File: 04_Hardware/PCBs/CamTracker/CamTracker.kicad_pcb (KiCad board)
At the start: 6 copper layers, 80 x 97.3 mm, 345 parts, among them IC1 W25Q128JVSIM, IC3 AP64502QSP-13, J1 PJ-059A, J10 67996-100HLF, J11 22-28-4044, J12 22-28-4044, J13 22-28-4044, J14 22-28-4044, J15 67996-100HLF, J16 SIM8066-6-1-14-01-A, J17 MEM2061-01-188-00-A, J18 636101112001, J19 636101112001, J2 22-28-4044, J20 636101112001, J21 636101112001, J22 22-28-4034, J23 22-28-4044, J24 22-28-4034, J25 1.25x15P, J26 1.25x15P, J27 53047-0210, J3 USB3076-30-A, J4 67996-100HLF, J5 USB4080-03-A, J6 22-28-4034, J7 22-28-4034, J8 67996-100HLF, J9 22-28-4034, Q1 BC817-40,215, Q10 BC817-40,215, Q11 BC817-40,215, Q12 BC817-40,215, Q2 BC817-40,215, Q4 BC817-40,215, Q5 BC817-40,215, Q6 BC817-40,215, Q7 BC817-40,215, Q8 BC817-40,215, Q9 BC817-40,215, U1 SC206EEMDA-G51-UGNDA, U2 SGM804, U3 AP7335-WG-7, U4 AP61100Z6-7, U5 PAM8302AASCR, U6 ST4SI2M0020TPIFW, U7 RP2040, U8 AP61100Z6-7, Y1 ABM8-272-T3

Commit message: feat: Completed Placement v1 in Layout
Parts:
- removed C38, C39, C49, C50, C72: 100nF 10V, 000MCLib:CAPC1005X55N
- removed C47: 22uF 6.3V, 000MCLib:CAPC1005X55N
- removed C48: 10uF 6.3V, 000MCLib:CAPC1005X55N
- removed C71, C76: 1uF 50V, 000MCLib:CAPC1005X55N
- removed C74: 47uF 10V X7S, 000MCLib:CAPC3225X280N
- removed D1: SMBJ20A, 000MCLib:DIOM5436X244N
- removed D10, D31: SP0402U-ULC-02ETG, 000MCLib:SESD0402Q2UG0020090
- removed D14, D15, D16, D32: SC1205-01ETG, 000MCLib:SC120501ETG
- removed D17: RB751S40, 000MCLib:SOD1608X70
- removed FL7, FL8: LCFE121002A900TG, 000MCLib:LCFE121002A900TG
- removed J19, J20: 636101112001, 000MCLib:COAX2_636101112001_WRE
- removed J25: 1.25x15P, 000MCLib:CONN-SMD_15P-P1.25_HCTL_HC-1.25-15PLT
- removed J8: 67996-100HLF, 000MCLib:HDRV2W67P254_2X1_254X483X858P
- removed L3: 74404024010, 000MCLib:IND_WE-LQS_2512_WRE
- removed Q12, Q7, Q8: BC817-40,215, 000MCLib:BC81740215
- removed R21: 0R, 000MCLib:RESC2012X50N
- removed R22, R47, R48, R51, R53, R86: 10K, 000MCLib:RC0402N_YAG
- removed R28: 1K, 000MCLib:RC0402N_YAG
- removed R50: 4K7, 000MCLib:RC0402N_YAG
- removed R88: 0R, 000MCLib:RC0402N_YAG
- removed REF**: Polarity_Center_Positive_6mm_SilkScreen, Symbol:Polarity_Center_Positive_6mm_SilkScreen
- removed TP56: TestPoint, TestPoint:TestPoint_Pad_D1.0mm
- removed U5: PAM8302AASCR, 000MCLib:SOP65P490X110-8N
- removed U8: AP61100Z6-7, 000MCLib:SOT50P162X60-6N
- added C100: 33pF 50V, 000MCLib:CAPC1005X55N, F.Cu at (163.6, 79.6)
- added C102: 100nF 10V, 000MCLib:CAPC1005X55N, F.Cu at (164.1, 82.2)
- added C103: 10pF 50V, 000MCLib:CAPC1005X55N, F.Cu at (164.6, 79.6)
- added C105: 22uF 6.3V, 000MCLib:CAPC1005X55N, F.Cu at (95.0, 67.1)
- added C108: 33pF 50V, 000MCLib:CAPC1005X55N, F.Cu at (97.5, 64.4)
- added C109: 33pF 50V, 000MCLib:CAPC1005X55N, F.Cu at (92.8, 63.3)
- added C110: 33pF 50V, 000MCLib:CAPC1005X55N, F.Cu at (97.5, 63.3)
- added C111: 100nF 10V, 000MCLib:CAPC1005X55N, B.Cu at (100.9, 95.3)
- added C112: 1uF 50V, 000MCLib:CAPC1005X55N, B.Cu at (101.9, 95.3)
- added C113: 1uF 50V, 000MCLib:CAPC1005X55N, B.Cu at (98.8, 99.5)
- added C114: 22uF 25V, 000MCLib:CAPC2012X145N, B.Cu at (188.6, 103.0)
- added C115: 100nF 10V, 000MCLib:CAPC1005X55N, B.Cu at (183.4, 104.7)
- added C116: 22uF 25V, 000MCLib:CAPC2012X145N, B.Cu at (185.4, 103.0)
- added C118: 220nF 10V, 000MCLib:CAPC1005X55N, B.Cu at (190.5, 69.5)
- added C119: 220nF 10V, 000MCLib:CAPC1005X55N, B.Cu at (190.5, 70.6)
- added C120: 220nF 10V, 000MCLib:CAPC1005X55N, B.Cu at (190.5, 71.7)
- added C121: 220nF 10V, 000MCLib:CAPC1005X55N, B.Cu at (190.5, 72.7)
- added C122: 10uF 50V X7R, 000MCLib:CAPC3216X190N, B.Cu at (190.7, 67.8)
- added C123: 10uF 50V X7R, 000MCLib:CAPC3216X190N, B.Cu at (190.7, 65.4)
- added C124: 10uF 50V X7R, 000MCLib:CAPC3216X190N, B.Cu at (190.7, 63.1)
- added C125: 100nF 10V, 000MCLib:CAPC1005X55N, B.Cu at (175.9, 63.9)
- added C126: 100nF 10V, 000MCLib:CAPC1005X55N, B.Cu at (176.7, 100.0)
- added C127: 100nF 10V, 000MCLib:CAPC1005X55N, B.Cu at (176.7, 86.8)
- added C128: 100nF 10V, 000MCLib:CAPC1005X55N, B.Cu at (190.1, 93.6)
- added C129: 100nF 10V, 000MCLib:CAPC1005X55N, B.Cu at (186.7, 100.4)
- added C130: 100nF 10V, 000MCLib:CAPC1005X55N, B.Cu at (174.0, 93.1)
- added C131: 100nF 10V, 000MCLib:CAPC1005X55N, B.Cu at (190.1, 91.2)
- added C132: 100nF 10V, 000MCLib:CAPC1005X55N, B.Cu at (184.0, 87.2)
- added C133: 100nF 10V, 000MCLib:CAPC1005X55N, B.Cu at (183.4, 102.9)
- added C134: 100nF 10V, 000MCLib:CAPC1005X55N, B.Cu at (174.1, 94.2)
- added C135: 100nF 10V, 000MCLib:CAPC1005X55N, B.Cu at (181.0, 86.1)
- added C136: 2.2uF 10V, 000MCLib:CAPC1608X90N, B.Cu at (190.3, 96.5)
- added C137: 22uF 25V, 000MCLib:CAPC2012X145N, B.Cu at (173.8, 86.8)
- added C138: 2.2uF 10V, 000MCLib:CAPC1608X90N, B.Cu at (190.3, 97.9)
- added C139: 100nF 10V, 000MCLib:CAPC1005X55N, B.Cu at (190.1, 95.3)
- added C140: 100nF 10V, 000MCLib:CAPC1005X55N, B.Cu at (190.1, 99.1)
- added C141: 100nF 10V, 000MCLib:CAPC1005X55N, B.Cu at (185.5, 100.4)
- added C142: 100nF 10V, 000MCLib:CAPC1005X55N, B.Cu at (174.0, 100.6)
- added C143: 220nF 10V, 000MCLib:CAPC1005X55N, B.Cu at (182.7, 100.4)
- added C144: 220nF 10V, 000MCLib:CAPC1005X55N, B.Cu at (181.7, 100.4)
- added C145: 220nF 10V, 000MCLib:CAPC1005X55N, B.Cu at (179.7, 100.4)
- added C146: 220nF 10V, 000MCLib:CAPC1005X55N, B.Cu at (180.7, 100.4)
- added C147: 100nF 10V, 000MCLib:CAPC1005X55N, B.Cu at (174.0, 99.6)
- added C148: 10pF 50V, 000MCLib:CAPC1005X55N, B.Cu at (171.2, 96.8)
- added C149: 1uF 50V, 000MCLib:CAPC1005X55N, B.Cu at (173.9, 89.5)
- added D19: SC1205-01ETG, 000MCLib:SC120501ETG, F.Cu at (117.6, 64.3)
- added D28: SC1205-01ETG, 000MCLib:SC120501ETG, F.Cu at (179.7, 87.6)
- added D29: SC1205-01ETG, 000MCLib:SC120501ETG, F.Cu at (193.1, 87.6)
- added FL4: LCFE121002A900TG, 000MCLib:LCFE121002A900TG, F.Cu at (178.7, 80.2)
- added FL5: LCFE121002A900TG, 000MCLib:LCFE121002A900TG, F.Cu at (178.7, 77.9)
- added IC2: AP7361E-33FGE-7, 000MCLib:SON65P300X300X63-9N, B.Cu at (116.2, 89.3)
- added J28: Bus_M.2_Socket_M, 000MCLib:121992304, B.Cu at (182.7, 72.0)
- added L10: 1uH 2.2A, 000MCLib:IND_WE-LQS_2512_WRE, B.Cu at (101.3, 90.0)
- added LED2: SML-P11VTT86R, 000MCLib:SMLP11VTT86R, F.Cu at (86.5, 64.5)
- added LED5: SML-P11VTT86R, 000MCLib:SMLP11VTT86R, B.Cu at (171.4, 91.9)
- added Q3: BC817-40,215, 000MCLib:BC81740215, F.Cu at (107.4, 67.0)
- added R113: 10K, 000MCLib:RC0402N_YAG, B.Cu at (189.9, 105.8)
- added R114: 10K, 000MCLib:RC0402N_YAG, B.Cu at (101.4, 87.5)
- added R115: 10K, 000MCLib:RC0402N_YAG, B.Cu at (173.9, 88.4)
- added R116: 10K, 000MCLib:RC0402N_YAG, B.Cu at (191.9, 91.7)
- added R117: 0R, 000MCLib:RC0402N_YAG, B.Cu at (190.1, 88.9)
- added R118: 0R, 000MCLib:RC0402N_YAG, B.Cu at (190.1, 90.1)
- added R119: 1K, 000MCLib:RC0402N_YAG, B.Cu at (172.7, 60.5)
- added R120: 10K, 000MCLib:RC0402N_YAG, B.Cu at (170.1, 61.7)
- added R121: 10K, 000MCLib:RC0402N_YAG, B.Cu at (190.3, 60.0)
- added R122: 0R, 000MCLib:RC0402N_YAG, B.Cu at (190.3, 61.3)
- added R123: 0R, 000MCLib:RC0402N_YAG, B.Cu at (172.8, 61.7)
- added R124: 4K7, 000MCLib:RC0402N_YAG, B.Cu at (190.1, 87.7)
- added R125: 12K1, 000MCLib:RC0402N_YAG, B.Cu at (175.7, 100.0)
- added R126: 100K, 000MCLib:RC0402N_YAG, B.Cu at (173.8, 90.7)
- added R127: 200K, 000MCLib:RC0402N_YAG, B.Cu at (98.1, 91.7)
- added R16: 0R, 000MCLib:RESC2012X50N, B.Cu at (109.6, 85.7)
- added R69: 33R, 000MCLib:RC0402N_YAG, F.Cu at (186.4, 89.9)
- added R73: 33R, 000MCLib:RC0402N_YAG, F.Cu at (190.4, 89.9)
- added R74: 10K, 000MCLib:RC0402N_YAG, F.Cu at (167.7, 87.3)
- added R75: 100K, 000MCLib:RC0402N_YAG, F.Cu at (169.7, 86.6)
- added R76: 51K, 000MCLib:RC0402N_YAG, F.Cu at (187.7, 89.9)
- added R77: 51K, 000MCLib:RC0402N_YAG, F.Cu at (182.4, 89.9)
- added R78: 51K, 000MCLib:RC0402N_YAG, F.Cu at (181.0, 89.9)
- added TP23: TestPoint, TestPoint:TestPoint_Pad_D1.0mm, F.Cu at (117.5, 74.4)
- added TP24: TestPoint, TestPoint:TestPoint_Pad_D1.0mm, F.Cu at (115.3, 74.4)
- added TP25: TestPoint, TestPoint:TestPoint_Pad_D1.0mm, F.Cu at (117.6, 72.3)
- added TP26: TestPoint, TestPoint:TestPoint_Pad_D1.0mm, F.Cu at (115.4, 72.3)
- added TP33: TestPoint, TestPoint:TestPoint_Pad_D1.0mm, B.Cu at (102.6, 99.8)
- added TP39: 3.86V, TestPoint:TestPoint_Pad_D1.0mm, B.Cu at (187.5, 96.3)
- added TP40: 3.86V, TestPoint:TestPoint_Pad_D1.0mm, B.Cu at (175.8, 84.9)
- added TP43: TestPoint, TestPoint:TestPoint_Pad_D1.0mm, B.Cu at (133.2, 66.9)
- added TP44: TestPoint, TestPoint:TestPoint_Pad_D1.0mm, B.Cu at (142.9, 100.9)
- added TP45: TestPoint, TestPoint:TestPoint_Pad_D1.0mm, B.Cu at (144.7, 99.9)
- added U10: SGM804, 000MCLib:SOT-23-5_L2.9-W1.6-P0.95-LS2.8-BL, F.Cu at (115.1, 68.8)
- added U11: ST4SI2M0020TPIFW, 000MCLib:SON127P600X500X100-9N, B.Cu at (166.2, 100.3)
- added U12: RP2040, 000MCLib:QFN40P700X700X90-57N-D, B.Cu at (137.5, 93.1)
- added U13: PAM8302AASCR, 000MCLib:SOP65P490X110-8N, F.Cu at (95.0, 71.6)
- added U14: ASM2362, 000MCLib:QFN50P905X905X75-65N, B.Cu at (181.2, 93.5)
- added U15: AP61100Z6-7, 000MCLib:SOT50P162X60-6N, B.Cu at (98.2, 89.9)
- added U9: PI3USB4000DZUAEX, 000MCLib:PI3USB4000DZUAEX, B.Cu at (98.8, 97.6)
- added Y2: 25MHz, 000MCLib:FL2500188, B.Cu at (173.5, 96.8)
- C1, C14, C2, C3, C35, C43, C44, C6, C84, D4, IC1, J1, Q10, Q11, R13, R17, R7, R82, R83, TP10, TP11, TP17, TP18, TP19, TP2, TP20, TP21, TP22, TP27, TP28, TP29, TP34, TP35, TP36, TP37, TP41, TP42, TP5, TP8, U3, Y1: moved to B.Cu
- C10, C61: value 47uF 10V X7S -> 33pF 50V; footprint 000MCLib:CAPC3225X280N -> 000MCLib:CAPC1005X55N
- C101: value 10uF 6.3V -> 100nF 10V
- C104, C54: value 33pF 50V -> 100nF 10V
- C107: value 33pF 50V -> 100pF 50V
- C11: value 100uF 10V -> 1uF 50V; footprint 000MCLib:T495D -> 000MCLib:CAPC1005X55N; moved to B.Cu
- C13, C51: value 100pF 50V -> 100nF 10V
- C15: value 22uF 6.3V -> 4.7uF 50V; footprint 000MCLib:CAPC1005X55N -> 000MCLib:CAP_UMK325B7475MM-T_TAY
- C16: value 1uF 50V -> 100uF 10V; footprint 000MCLib:CAPC1005X55N -> 000MCLib:T495D
- C17: value 33pF 50V -> 47uF 10V X7S; footprint 000MCLib:CAPC1005X55N -> 000MCLib:CAPC3225X280N; moved to B.Cu
- C18, C20: value 1uF 50V -> 47uF 10V X7S; footprint 000MCLib:CAPC1005X55N -> 000MCLib:CAPC3225X280N; moved to B.Cu
- C19: value 100nF 10V -> 47uF 10V X7S; footprint 000MCLib:CAPC1005X55N -> 000MCLib:CAPC3225X280N; moved to B.Cu
- C21: value 100nF 10V -> 1uF 50V; moved to B.Cu
- C22: value 10uF 50V X7R -> 100nF 10V; footprint 000MCLib:CAPC3216X190N -> 000MCLib:CAPC1005X55N; moved to B.Cu
- C23: value 10uF 6.3V -> 10uF 50V X7R; footprint 000MCLib:CAPC1005X55N -> 000MCLib:CAPC3216X190N; moved to B.Cu
- C24: value 220nF 10V -> 100nF 50V X7R; moved to B.Cu
- C25: value 330nF 10V -> 10uF 50V X7R; footprint 000MCLib:CAPC1005X55N -> 000MCLib:CAPC3216X190N; moved to B.Cu
- C26: value 100nF 10V -> 10uF 50V X7R; footprint 000MCLib:CAPC1005X55N -> 000MCLib:CAPC3216X190N; moved to B.Cu
- C27: value 4.7uF 10V -> 10uF 50V X7R; footprint 000MCLib:CAPC1608X90N -> 000MCLib:CAPC3216X190N; moved to B.Cu
- C28: value 220nF 10V -> 47uF 10V X7S; footprint 000MCLib:CAPC1005X55N -> 000MCLib:CAPC3225X280N; moved to B.Cu
- C29, C31: value 330nF 10V -> 1uF 50V; moved to B.Cu
- C30: value 330nF 10V -> 100nF 10V; moved to B.Cu
- C32: value 220nF 10V -> 100nF 10V; moved to B.Cu
- C33: value 220nF 10V -> 10uF 50V X7R; footprint 000MCLib:CAPC1005X55N -> 000MCLib:CAPC3216X190N; moved to B.Cu
- C34: value 1uF 50V -> 10uF 50V X7R; footprint 000MCLib:CAPC1005X55N -> 000MCLib:CAPC3216X190N; moved to B.Cu
- C36: value 100nF 10V -> 220uF 16V; footprint 000MCLib:CAPC1005X55N -> 000MCLib:CAPAE830X1000N
- C37: value 1uF 50V -> 10pF 50V
- C4: value 10uF 50V X7R -> 100nF 50V X7R; footprint 000MCLib:CAPC3216X190N -> 000MCLib:CAPC1005X55N; moved to B.Cu
- C42: value 1uF 50V -> 4.7uF 10V; footprint 000MCLib:CAPC1005X55N -> 000MCLib:CAPC1608X90N
- C45: value 33pF 50V -> 1uF 50V; moved to B.Cu
- C46: value 47uF 10V X7S -> 100nF 10V; footprint 000MCLib:CAPC3225X280N -> 000MCLib:CAPC1005X55N; moved to B.Cu
- C5: value 100nF 50V X7R -> 22uF 6.3V
- C52, C57, C59, C60, C73: value 100nF 10V -> 1uF 50V
- C53: value 1uF 50V -> 100nF 10V
- C62, C64: value 100nF 10V -> 22pF 50V
- C63: value 15pF 50V -> 22pF 50V
- C65: value 15pF 50V -> 100nF 10V
- C66: value 4.7uF 50V -> 47uF 10V X7S; footprint 000MCLib:CAP_UMK325B7475MM-T_TAY -> 000MCLib:CAPC3225X280N
- C67: value 1nF 50V -> 22pF 50V; moved to B.Cu
- C68: value 1nF 50V -> 33pF 50V
- C69, C70: value 100nF 10V -> 22pF 50V; moved to B.Cu
- C7: value 100nF 50V X7R -> 1uF 50V
- C77, C79: value 100nF 10V -> 33pF 50V; moved to F.Cu
- C78: value 1uF 50V -> 33pF 50V; moved to F.Cu
- C8: value 10nF 50V -> 33pF 50V
- C80: value 1uF 50V -> 100pF 50V; moved to F.Cu
- C81: value 22pF 50V -> 33pF 50V
- C82, C83: value 22pF 50V -> 15pF 50V; moved to B.Cu
- C85: value 22pF 50V -> 100nF 10V; moved to B.Cu
- C86, C87: value 22pF 50V -> 1uF 50V; moved to B.Cu
- C88, C89, C90, C91, C92, C93, C94, C95: value 33pF 50V -> 100nF 10V; moved to B.Cu
- C9: value 47uF 10V X7S -> 10nF 50V; footprint 000MCLib:CAPC3225X280N -> 000MCLib:CAPC1005X55N; moved to B.Cu
- C96, C97: value 33pF 50V -> 1nF 50V; moved to B.Cu
- C98: value 10pF 50V -> 10uF 6.3V
- C99: value 100pF 50V -> 10uF 6.3V
- D12: value SP0402U-ULC-02ETG -> SC1105-01UTG; footprint 000MCLib:SESD0402Q2UG0020090 -> 000MCLib:SC110501UTG
- D13, D8: value SP0402U-ULC-02ETG -> B550C-13-F; footprint 000MCLib:SESD0402Q2UG0020090 -> 000MCLib:DIOM7959X250N
- D18: value SC1205-01ETG -> SP0402U-ULC-02ETG; footprint 000MCLib:SC120501ETG -> 000MCLib:SESD0402Q2UG0020090; moved to B.Cu
- D2: value SC1122-01UTG -> SMBJ20A; footprint 000MCLib:SC110501UTG -> 000MCLib:DIOM5436X244N; moved to B.Cu
- D20: value SRV05-4.TCT -> SC1205-01ETG; footprint 000MCLib:SOT95P280X145-6N -> 000MCLib:SC120501ETG
- D24: value SC1205-01ETG -> SRV05-4.TCT; footprint 000MCLib:SC120501ETG -> 000MCLib:SOT95P280X145-6N
- D3: value B550C-13-F -> SC1122-01UTG; footprint 000MCLib:DIOM7959X250N -> 000MCLib:SC110501UTG; moved to B.Cu
- D30, D9: value SP0402U-ULC-02ETG -> SC1205-01ETG; footprint 000MCLib:SESD0402Q2UG0020090 -> 000MCLib:SC120501ETG
- D5: value ESD9B5.0ST5G -> RB751S40; footprint 000MCLib:SODFL1006X40N -> 000MCLib:SOD1608X70
- D7: value SC1105-01UTG -> ESD9B5.0ST5G; footprint 000MCLib:SC110501UTG -> 000MCLib:SODFL1006X40N
- FL6, L6, L7, R60: moved to F.Cu
- IC3: value AP64502QSP-13 -> AP7361E-33FGE-7; footprint 000MCLib:SOIC127P600X163-9N -> 000MCLib:SON65P300X300X63-9N; moved to B.Cu
- J10: value 67996-100HLF -> 1.25x15P; footprint 000MCLib:HDRV2W67P254_2X1_254X483X858P -> 000MCLib:CONN-SMD_15P-P1.25_HCTL_HC-1.25-15PLT
- J11: value 22-28-4044 -> 22-28-4034; footprint 000MCLib:HDRV3W66P0X254_1X4_762X249X1042P -> 000MCLib:HDRV3W66P0X254_1X3_762X249X1042P
- J12: value 22-28-4044 -> 22-28-4034; footprint 000MCLib:HDRV3W66P0X254_1X4_762X249X1042P -> 000MCLib:HDRV3W66P0X254_1X3_762X249X1042P; moved to B.Cu
- J13: value 22-28-4044 -> SIM8066-6-1-14-01-A; footprint 000MCLib:HDRV3W66P0X254_1X4_762X249X1042P -> 000MCLib:SIM8066611401A
- J14: value 22-28-4044 -> MEM2061-01-188-00-A; footprint 000MCLib:HDRV3W66P0X254_1X4_762X249X1042P -> 000MCLib:MEM20610118800A
- J15: value 67996-100HLF -> 636101112001; footprint 000MCLib:HDRV2W67P254_2X1_254X483X858P -> 000MCLib:COAX2_636101112001_WRE; moved to F.Cu
- J16: value SIM8066-6-1-14-01-A -> 636101112001; footprint 000MCLib:SIM8066611401A -> 000MCLib:COAX2_636101112001_WRE
- J17: value MEM2061-01-188-00-A -> 636101112001; footprint 000MCLib:MEM20610118800A -> 000MCLib:COAX2_636101112001_WRE
- J2: value 22-28-4044 -> 67996-100HLF; footprint 000MCLib:HDRV3W66P0X254_1X4_762X249X1042P -> 000MCLib:HDRV2W67P254_2X1_254X483X858P; moved to B.Cu
- J21: value 636101112001 -> 67996-100HLF; footprint 000MCLib:COAX2_636101112001_WRE -> 000MCLib:HDRV2W67P254_2X1_254X483X858P; moved to B.Cu
- J22: value 22-28-4034 -> USB3076-30-A; footprint 000MCLib:HDRV3W66P0X254_1X3_762X249X1042P -> 000MCLib:USB307630A; moved to B.Cu
- J23: value 22-28-4044 -> ~; footprint 000MCLib:HDRV3W66P0X254_1X4_762X249X1042P -> 000MCLib:CONN-SMD_1.25-4PLT; moved to B.Cu
- J24: value 22-28-4034 -> ~; footprint 000MCLib:HDRV3W66P0X254_1X3_762X249X1042P -> 000MCLib:CONN-SMD_1.25-4PLT; moved to B.Cu
- J26: value 1.25x15P -> ~; footprint 000MCLib:CONN-SMD_15P-P1.25_HCTL_HC-1.25-15PLT -> 000MCLib:CONN-SMD_1.25-4PLT; moved to B.Cu
- J3: value USB3076-30-A -> 67996-100HLF; footprint 000MCLib:USB307630A -> 000MCLib:HDRV2W67P254_2X1_254X483X858P
- J4: value 67996-100HLF -> ~; footprint 000MCLib:HDRV2W67P254_2X1_254X483X858P -> 000MCLib:CONN-SMD_1.25-4PLT; moved to B.Cu
- J5: value USB4080-03-A -> 22-28-4034; footprint 000MCLib:GCT_USB4080-03-A_REVA -> 000MCLib:HDRV3W66P0X254_1X3_762X249X1042P
- J6: value 22-28-4034 -> USB4080-03-A; footprint 000MCLib:HDRV3W66P0X254_1X3_762X249X1042P -> 000MCLib:GCT_USB4080-03-A_REVA; moved to B.Cu
- J7: value 22-28-4034 -> 22-28-4044; footprint 000MCLib:HDRV3W66P0X254_1X3_762X249X1042P -> 000MCLib:HDRV3W66P0X254_1X4_762X249X1042P
- J9: value 22-28-4034 -> 1.25x15P; footprint 000MCLib:HDRV3W66P0X254_1X3_762X249X1042P -> 000MCLib:CONN-SMD_15P-P1.25_HCTL_HC-1.25-15PLT
- L1: value ETQ-P4M6R8KVK 6.8uH 6.9A -> ETQ-P4M6R8KVC 6.8uH 6.9A; footprint 000MCLib:ETQ-P4M_KVK -> 000MCLib:ETQ-P4M_KVC; moved to B.Cu
- L2: value 56nH -> 1uH 4.2A; footprint 000MCLib:INDC1005X60N -> 000MCLib:LSEUC3225HKT1R0M; moved to B.Cu
- L5: value 74404024010 -> 600ohm 100MHz; footprint 000MCLib:IND_WE-LQS_2512_WRE -> 000MCLib:0402
- L8: value 600ohm 100MHz -> 56nH; footprint 000MCLib:0402 -> 000MCLib:INDC1005X60N
- LED1: value SML-P11VTT86R -> SML-P11YTT86R; moved to B.Cu
- LED3: value SML-P11YTT86R -> LTPL-C0676WPGB; footprint 000MCLib:SMLP11VTT86R -> 000MCLib:LTPL-C0676WPGB
- LED4: value LTPL-C0676WPGB -> SML-P11VTT86R; footprint 000MCLib:LTPL-C0676WPGB -> 000MCLib:SMLP11VTT86R
- R1: value 200K -> 0R
- R10: value 10K -> 47K; moved to B.Cu
- R102: value 10K -> 0R
- R104: value 10K -> 56K; moved to B.Cu
- R105: footprint 000MCLib:RC0402N_YAG -> 000MCLib:RESC2012X50N; moved to B.Cu
- R106: value 0R -> 10K; moved to B.Cu
- R107: value 0R -> 200K; moved to B.Cu
- R108: value 0R -> 44K2; moved to B.Cu
- R109: value 47K -> 5K1; moved to B.Cu
- R11: value 147K -> 4K7; moved to B.Cu
- R110, R91: value 10K -> 1K; moved to B.Cu
- R111: value 10K -> 5K1; moved to B.Cu
- R12: value 47K -> 0R; footprint 000MCLib:RC0402N_YAG -> 000MCLib:RESC2012X50N; moved to B.Cu
- R14: value 2K2 -> 0R; footprint 000MCLib:RC0402N_YAG -> 000MCLib:RESC2012X50N; moved to B.Cu
- R15, R8: value 0R -> 10K; footprint 000MCLib:RESC2012X50N -> 000MCLib:RC0402N_YAG; moved to B.Cu
- R18: value 10K -> 12K1; moved to B.Cu
- R19: value 220K -> 0R; footprint 000MCLib:RC0402N_YAG -> 000MCLib:RESC2012X50N; moved to B.Cu
- R2: value 10K -> 47K
- R20, R31: value 10K -> 0R; footprint 000MCLib:RC0402N_YAG -> 000MCLib:RESC2012X50N
- R23, R24: value 220K -> 10K
- R25: value 220K -> 4K7; moved to B.Cu
- R26: value 2K2 -> 10K
- R27: value 10K -> 270K; moved to B.Cu
- R29: value 44K2 -> 10K
- R3: value 38K3 -> 200K; moved to B.Cu
- R32, R39: value 10K -> 1K
- R33: value 27.4R -> 4K7
- R34: value 27.4R -> 20K
- R35: value 10K -> 27K
- R36: value 200K -> 1K
- R37: value 44K2 -> 1K
- R4: value 4K7 -> 38K3; moved to B.Cu
- R40, R42, R43: value 1K -> 10K
- R45: value 4K7 -> 10K
- R5: value 2K2 -> 10K; moved to B.Cu
- R52: value 27K -> 10K
- R55, R56, R57: value 1K -> 0R; footprint 000MCLib:RC0402N_YAG -> 000MCLib:RESC2012X50N
- R58: footprint 000MCLib:RC0402N_YAG -> 000MCLib:RESC2012X50N
- R59: value 20K -> 2K2
- R61: value 4K7 -> 2K2
- R62: value 0R -> 2K2; footprint 000MCLib:RESC2012X50N -> 000MCLib:RC0402N_YAG
- R63: value 0R -> 1K; footprint 000MCLib:RESC2012X50N -> 000MCLib:RC0402N_YAG
- R64: value 51K -> 100K
- R65, R67: value 51K -> 22R
- R66: value 200K -> 22R
- R68, R70: value 51K -> 33R
- R71: value 1K -> 33R
- R72: value 100K -> 33R
- R79, R80: value 0R -> 51K; footprint 000MCLib:RESC2012X50N -> 000MCLib:RC0402N_YAG
- R81: value 0R -> 22R; footprint 000MCLib:RESC2012X50N -> 000MCLib:RC0402N_YAG
- R84: value 22R -> 10K; moved to B.Cu
- R85: value 100K -> 0R; moved to B.Cu
- R87: value 22R -> 0R; footprint 000MCLib:RC0402N_YAG -> 000MCLib:RESC2012X50N
- R89, R90: value 22R -> 0R
- R9: value 0R -> 147K; moved to B.Cu
- R92, R97: value 33R -> 10K; moved to B.Cu
- R93, R94: value 33R -> 27.4R; moved to B.Cu
- R95: value 33R -> 1K; moved to B.Cu
- R96: value 33R -> 4K7; moved to B.Cu
- R98: value 0R -> 10K; footprint 000MCLib:RESC2012X50N -> 000MCLib:RC0402N_YAG
- R99: value 10K -> 4K7; moved to B.Cu
- TP1: value 3.86V -> TestPoint
- TP15, TP16, TP38, TP9: value TestPoint -> 3.86V; moved to B.Cu
- U2: value SGM804 -> AP64502QSP-13; footprint 000MCLib:SOT-23-5_L2.9-W1.6-P0.95-LS2.8-BL -> 000MCLib:SOIC127P600X163-9N; moved to B.Cu
- U4: value AP61100Z6-7 -> AP22654QWU-7; footprint 000MCLib:SOT50P162X60-6N -> 000MCLib:SOT95P280X82-6N; moved to B.Cu
- U6: value ST4SI2M0020TPIFW -> AP61300Z6-7; footprint 000MCLib:SON127P600X500X100-9N -> 000MCLib:SOT50P162X60-6N; moved to B.Cu
- U7: value RP2040 -> PI3USB4000DZUAEX; footprint 000MCLib:QFN40P700X700X90-57N-D -> 000MCLib:PI3USB4000DZUAEX; moved to B.Cu
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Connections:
- C1 pad 1: Net-(D3-K) -> Net-(C36-+)
- C10 pad 1: VREG_3V8 -> VBAT
- C101 pad 1: Net-(U1H-LINEOUT_M) -> /Audio/MIC1_P
- C101 pad 2: Net-(C101-Pad2) -> Net-(MK1-OUTPUT)
- C104 pad 1: GND -> Net-(MK1-VDD)
- C104 pad 2: Net-(U5-VO+) -> GND
- C106 pad 2: Net-(C106-Pad2) -> Net-(U13-VO-)
- C107 pad 1: GND -> Net-(U13-VO-)
- C107 pad 2: Net-(C107-Pad2) -> Net-(U13-VO+)
- C11 pad 1: VBAT -> 3V8
- C12 pad 1: VBAT -> Net-(C12-Pad1)
- C14 pad 1: Net-(C14-Pad1) -> 3V8
- C17 pad 1: VBAT -> 3V8
- C18 pad 1: VREG_3V8 -> 3V8
- C19 pad 1: VREG_3V8 -> 3V8
- C2 pad 1: Net-(D3-K) -> Net-(C36-+)
- C20 pad 1: VREG_3V3 -> 3V8
- C22 pad 1: VPH_PWR -> VREG_3V3
- C23 pad 1: GND -> TypeC_VBUS
- C23 pad 2: CAM1_3V3 -> GND
- C24 pad 1: /USB_UARTs/USB_SS1_TX_P -> TypeC_VBUS
- C24 pad 2: /USB_UARTs/USB_SS_TX1_P -> GND
- C25 pad 1: /USB_UARTs/USB_SS2_RX_N -> VPH_PWR
- C25 pad 2: /USB_UARTs/USB_SS_RX2_N -> GND
- C26 pad 1: VUSB_BUS -> VPH_PWR
- C27 pad 1: VUSB_BUS -> 3V8
- C28 pad 1: /USB_UARTs/USB_SS1_TX_N -> NVMe_3V3
- C28 pad 2: /USB_UARTs/USB_SS_TX1_N -> GND
- C29 pad 1: /USB_UARTs/USB_SS2_RX_P -> NVMe_3V3
- C29 pad 2: /USB_UARTs/USB_SS_RX2_P -> GND
- C3 pad 1: Net-(D3-K) -> Net-(C36-+)
- C30 pad 1: /USB_UARTs/USB_SS_RX1_P -> NVMe_3V3
- C30 pad 2: /USB_UARTs/USB_SS1_RX_P -> GND
- C31 pad 1: /USB_UARTs/USB_SS_RX1_N -> 3V8
- C31 pad 2: /USB_UARTs/USB_SS1_RX_N -> GND
- C32 pad 1: /USB_UARTs/USB_SS_TX2_N -> 3V8
- C32 pad 2: /USB_UARTs/USB_SS2_TX_N -> GND
- C33 pad 1: /USB_UARTs/USB_SS_TX2_P -> CAM0_3V3
- C33 pad 2: /USB_UARTs/USB_SS2_TX_P -> GND
- C34 pad 1: VUSB_BUS -> CAM1_3V3
- C35 pad 1: CAM1_3V3 -> Net-(U7-REF)
- C36 pad 1: CAM1_3V3 -> Net-(C36-+)
- C37 pad 1: CAM0_3V3 -> VBAT
- C4 pad 1: VUSB_BUS -> Net-(C36-+)
- C40 pad 1: /Cameras/CAM1_3V3_1 -> VUSB_BUS
- C41 pad 1: /Cameras/CAM1_3V3_0 -> VUSB_BUS
- C42 pad 1: /Cameras/CAM1_3V3_1 -> VUSB_BUS
- C43 pad 1: VPH_PWR -> 3V8
- C44 pad 2: CAM0_3V3 -> NVMe_1V05
- C45 pad 1: GND -> NVMe_1V05
- C45 pad 2: /SIM_SD/SD_CD -> GND
- C46 pad 1: /SIM_SD/SD_VDD -> NVMe_1V05
- C5 pad 1: Net-(D3-K) -> VBAT
- C51 pad 1: /Antennas/ANT_GNSS_C0 -> VBAT
- C51 pad 2: /Antennas/ANT_GNSS_C1 -> GND
- C52 pad 1: /Audio/MIC1_M -> Net-(U10-SRT)
- C52 pad 2: Net-(MK1-GND_1) -> GND
- C53 pad 1: Net-(C53-Pad1) -> /Cameras/CAM0_3V3_0
- C54 pad 1: /Audio/MIC1_P -> /Cameras/CAM0_3V3_1
- C55 pad 1: Net-(C53-Pad1) -> /Cameras/CAM1_3V3_0
- C56 pad 1: VREG_3V3 -> /Cameras/CAM1_3V3_1
- C57 pad 1: VREG_3V3 -> /Cameras/CAM0_3V3_0
- C58 pad 1: VREG_3V3 -> /Cameras/CAM0_3V3_1
- C59 pad 1: VREG_3V3 -> /Cameras/CAM1_3V3_0
- C6 pad 1: VUSB_BUS -> Net-(U2-BST)
- C6 pad 2: GND -> Net-(U2-SW)
- C60 pad 1: VREG_3V3 -> /Cameras/CAM1_3V3_1
- C61 pad 1: VREG_3V8 -> GND
- C61 pad 2: GND -> /SIM_SD/SD_CD
- C62 pad 1: VREG_3V3 -> GND
- C62 pad 2: GND -> Net-(D24-I/O3)
- C63 pad 1: Net-(U7-XIN) -> GND
- C63 pad 2: GND -> Net-(D24-I/O2)
- C64 pad 1: VREG_3V3 -> GND
- C64 pad 2: GND -> Net-(D24-I/O1)
- C65 pad 1: Net-(C65-Pad1) -> /SIM_SD/USIM1_VDD
- C66 pad 1: VBAT -> /SIM_SD/SD_VDD
- C67 pad 1: Net-(Q2-B) -> Net-(U11-CLK)
- C67 pad 2: LDO15A_1V8 -> GND
- C68 pad 1: Net-(Q12-B) -> /SIM_SD/SD_VDD
- C68 pad 2: LDO15A_1V8 -> GND
- C69 pad 1: VREG_3V3 -> Net-(U11-~{RESET})
- C7 pad 1: Net-(IC3-BST) -> VBAT
- C7 pad 2: Net-(IC3-SW) -> GND
- C70 pad 1: VREG_3V3 -> Net-(U11-I/O)
- C73 pad 1: Net-(U7-VREG_VOUT) -> Net-(C73-Pad1)
- C75 pad 1: VBAT -> Net-(C73-Pad1)
- C77 pad 1: /Cameras/CAM0_3V3_0 -> /Antennas/ANT_GNSS
- C78 pad 1: /Cameras/CAM0_3V3_0 -> /Antennas/ANT_DRX
- C79 pad 1: /Cameras/CAM0_3V3_1 -> /Antennas/ANT_GNSS_C0
- C8 pad 1: Net-(IC3-SS) -> VBAT
- C80 pad 1: /Cameras/CAM0_3V3_1 -> /Antennas/ANT_GNSS_C0
- C80 pad 2: GND -> /Antennas/ANT_GNSS_C1
- C81 pad 1: GND -> /Antennas/ANT_DRX_C
- C81 pad 2: Net-(D20-I/O3) -> GND
- C82 pad 1: GND -> Net-(U12-XIN)
- C82 pad 2: Net-(D20-I/O2) -> GND
- C83 pad 1: GND -> Net-(C83-Pad1)
- C83 pad 2: Net-(D20-I/O1) -> GND
- C84 pad 1: /SIM_SD/USIM1_VDD -> Net-(U12-VREG_VOUT)
- C85 pad 1: Net-(U6-CLK) -> Net-(U12-VREG_VOUT)
- C86 pad 1: Net-(U6-~{RESET}) -> Net-(U12-VREG_VOUT)
- C87 pad 1: Net-(U6-I/O) -> VREG_3V3
- C88 pad 1: GND -> VREG_3V3
- C88 pad 2: Net-(U5-VO-) -> GND
- C89 pad 1: /SIM_SD/SD_VDD -> VREG_3V3
- C9 pad 1: VREG_3V8 -> Net-(U2-SS)
- C90 pad 1: /Antennas/ANT_MAIN_C -> VREG_3V3
- C91 pad 1: /Antennas/ANT_MAIN -> VREG_3V3
- C92 pad 1: /Antennas/ANT_DRX -> VREG_3V3
- C93 pad 1: /Antennas/ANT_DRX_C -> VREG_3V3
- C94 pad 1: /Antennas/ANT_GNSS -> VREG_3V3
- C95 pad 1: /Antennas/ANT_GNSS_C0 -> VREG_3V3
- C96 pad 1: /Antennas/ANT_WiFi -> Net-(Q10-B)
- C96 pad 2: GND -> LDO15A_1V8
- C97 pad 1: /Antennas/ANT_WiFi_C0 -> Net-(Q11-B)
- C97 pad 2: GND -> LDO15A_1V8
- C98 pad 1: Net-(MK1-OUTPUT) -> Net-(U1H-LINEOUT_P)
- C98 pad 2: GND -> Net-(C98-Pad2)
- C99 pad 1: Net-(U5-VO-) -> Net-(U1H-LINEOUT_M)
- C99 pad 2: Net-(U5-VO+) -> Net-(C99-Pad2)
- D11 pad 1: /USB_UARTs/USB_SS_TX1_N -> Net-(D11-K_1)
- D11 pad 2: /USB_UARTs/USB_SS_TX1_P -> Net-(D11-K_2)
- D12 pad 1: /USB_UARTs/USB_D_N -> VUSB_BUS
- D12 pad 2: /USB_UARTs/USB_D_P -> GND
- D13 pad 1: /USB_UARTs/CC2 -> VUSB_BUS
- D13 pad 2: /USB_UARTs/CC1 -> TypeC_VBUS
- D18 pad 1: /SIM_SD/SD_CD -> /USB_UARTs/TypeC_USB_D_N
- D18 pad 2: GND -> /USB_UARTs/TypeC_USB_D_P
- D2 pad 1: Net-(D1-K) -> Net-(D2-K)
- D20 pad 1: Net-(D20-I/O1) -> GND
- D20 pad 2: GND -> Net-(D20-Pad2)
- D21 pad 1: /SIM_SD/SD_VDD -> GND
- D21 pad 2: GND -> Net-(D21-Pad2)
- D22 pad 1: Net-(J17-CLK) -> /SIM_SD/SD_CD
- D23 pad 1: Net-(J17-CMD) -> /SIM_SD/SD_VDD
- D24 pad 1: Net-(J17-DAT0) -> Net-(D24-I/O1)
- D25 pad 1: Net-(J17-DAT1) -> Net-(J14-CLK)
- D26 pad 1: Net-(J17-DAT2) -> Net-(J14-CMD)
- D27 pad 1: Net-(J17-CD/DAT3) -> Net-(J14-DAT0)
- D3 pad 1: Net-(D3-K) -> Net-(D2-K)
- D3 pad 2: Net-(D1-K) -> GND
- D30 pad 1: Net-(D30-K_1) -> Net-(J14-CD/DAT3)
- D30 pad 2: Net-(D30-K_2) -> GND
- D4 pad 1: Net-(D3-K) -> Net-(C36-+)
- D4 pad 2: VUSB_BUS -> Net-(D2-K)
- D5 pad 1: VBAT -> Net-(C12-Pad1)
- D5 pad 2: GND -> VREG_3V3
- D7 pad 1: VUSB_BUS -> VBAT
- D8 pad 1: /USB_UARTs/USB_SS_RX2_P -> Net-(C36-+)
- D8 pad 2: /USB_UARTs/USB_SS_RX2_N -> TypeC_VBUS
- D9 pad 1: /USB_UARTs/USB_SS_TX2_N -> Net-(U1E-USB_BOOT)
- D9 pad 2: /USB_UARTs/USB_SS_TX2_P -> GND
- FB1 pad 1: Net-(U5-VO-) -> Net-(MK1-VDD)
- FB1 pad 2: Net-(C106-Pad2) -> /Audio/MIC_BIAS1
- FB2 pad 1: Net-(U5-VO+) -> Net-(U13-VO-)
- FB2 pad 2: Net-(C107-Pad2) -> Net-(C109-Pad2)
- FB3 pad 1: Net-(MK1-VDD) -> Net-(U13-VO+)
- FB3 pad 2: /Audio/MIC_BIAS1 -> Net-(C110-Pad2)
- FL1 pad 1: /Cameras/CSI1_LN0_N -> /Cameras/CSI0_LN0_N
- FL1 pad 2: /Cameras/CSI1_LN0_P -> /Cameras/CSI0_LN0_P
- FL1 pad 3: /Cameras/CAM1_MD0_P -> /Cameras/CAM0_MD0_P
- FL1 pad 4: /Cameras/CAM1_MD0_N -> /Cameras/CAM0_MD0_N
- FL2 pad 1: /Cameras/CSI1_LN1_N -> /Cameras/CSI0_LN1_N
- FL2 pad 2: /Cameras/CSI1_LN1_P -> /Cameras/CSI0_LN1_P
- FL2 pad 3: /Cameras/CAM1_MD1_P -> /Cameras/CAM0_MD1_P
- FL2 pad 4: /Cameras/CAM1_MD1_N -> /Cameras/CAM0_MD1_N
- FL3 pad 1: /Cameras/CSI1_CLK_N -> /Cameras/CSI0_CLK_N
- FL3 pad 2: /Cameras/CSI1_CLK_P -> /Cameras/CSI0_CLK_P
- FL3 pad 3: /Cameras/CAM1_CLK_P -> /Cameras/CAM0_CLK_P
- FL3 pad 4: /Cameras/CAM1_CLK_N -> /Cameras/CAM0_CLK_N
- FL6 pad 1: /Cameras/CSI0_CLK_N -> /Cameras/CSI1_CLK_P
- FL6 pad 2: /Cameras/CSI0_CLK_P -> /Cameras/CSI1_CLK_N
- FL6 pad 3: /Cameras/CAM0_CLK_P -> /Cameras/CAM1_CLK_N
- FL6 pad 4: /Cameras/CAM0_CLK_N -> /Cameras/CAM1_CLK_P
- IC3 pad 1: Net-(IC3-BST) -> CAM1_3V3
- IC3 pad 2: Net-(D3-K) -> unconnected-(IC3-NC_1-Pad2)
- IC3 pad 3: Net-(D3-K) -> unconnected-(IC3-ADJ/NC-Pad3)
- IC3 pad 4: Net-(IC3-RT/CLK) -> GND
- IC3 pad 5: /Power/FB -> Net-(IC3-EN)
- IC3 pad 6: Net-(IC3-SS) -> unconnected-(IC3-NC_2-Pad6)
- IC3 pad 7: GND -> unconnected-(IC3-PG-Pad7)
- IC3 pad 8: Net-(IC3-SW) -> VPH_PWR
- J1 pad 1: Net-(D1-K) -> Net-(D2-K)
- J10 pad 1: Net-(U1E-USB_BOOT) -> /Cameras/CAM1_MD0_N
- J10 pad 2: Net-(J10-Pad2) -> /Cameras/CAM1_MD0_P
- J11 pad 1: /MCU/GPIO4 -> /Cameras/CAM0_PWDN
- J11 pad 2: /MCU/GPIO5 -> /Cameras/CAM0_MCLK
- J11 pad 3: /MCU/GPIO6 -> /Cameras/CAM0_RST
- J12 pad 1: /MCU/GPIO12 -> /Cameras/CAM1_PWDN
- J12 pad 2: /MCU/GPIO13 -> /Cameras/CAM1_MCLK
- J12 pad 3: /MCU/GPIO14 -> /Cameras/CAM1_RST
- J15 pad 1: GND -> /Antennas/ANT_MAIN
- J15 pad 2: /MCU/RUN -> GND
- J18 pad 1: /Antennas/ANT_MAIN_C -> /Antennas/ANT_DRX_C
- J2 pad 1: /Interfaces/IN1 -> VBAT
- J2 pad 2: /Interfaces/IN2 -> 3V8
- J21 pad 1: /Antennas/ANT_WiFi_C0 -> GND
- J21 pad 2: GND -> /MCU/USB_BOOT
- J22 pad 1: /MCU/SWD -> Net-(J22-Pad1)
- J22 pad 2: GND -> Net-(J22-Pad2)
- J22 pad 3: /MCU/SWCLK -> Net-(J22-Pad3)
- J23 pad 1: /Interfaces/OUT1 -> /MCU/GPIO4
- J23 pad 2: /Interfaces/OUT2 -> /MCU/GPIO5
- J23 pad 3: VREG_3V8 -> /MCU/GPIO6
- J23 pad 4: GND -> /MCU/GPIO7
- J24 pad 1: /Cameras/CAM1_PWDN -> /MCU/GPIO12
- J24 pad 2: /Cameras/CAM1_MCLK -> /MCU/GPIO13
- J24 pad 3: /Cameras/CAM1_RST -> /MCU/GPIO14
- J26 pad 1: /Cameras/CAM1_MD0_N -> /MCU/ADC0
- J26 pad 2: /Cameras/CAM1_MD0_P -> /MCU/ADC1
- J26 pad 3: GND -> /MCU/ADC2
- J26 pad 4: /Cameras/CAM1_MD1_N -> /MCU/ADC3
- J26 pad 5: /Cameras/CAM1_MD1_P -> GND
- J27 pad 1: Net-(C107-Pad2) -> Net-(C110-Pad2)
- J27 pad 2: Net-(C106-Pad2) -> Net-(C109-Pad2)
- J3 pad 1: Net-(J3-Pad1) -> Net-(U1E-USB_BOOT)
- J4 pad 1: VBAT -> /MCU/SWCLK
- J4 pad 2: VREG_3V8 -> /MCU/SWD
- J7 pad 1: /Cameras/CAM0_PWDN -> /Interfaces/IN1
- J7 pad 2: /Cameras/CAM0_MCLK -> /Interfaces/OUT1
- J7 pad 3: /Cameras/CAM0_RST -> /Interfaces/ADC
- J9 pad 1: Net-(D31-K_2) -> /Cameras/CAM0_MD0_N
- J9 pad 2: Net-(D31-K_1) -> /Cameras/CAM0_MD0_P
- L1 pad 1: Net-(IC3-SW) -> Net-(U2-SW)
- L1 pad 2: VREG_3V8 -> 3V8
- L2 pad 1: Net-(C53-Pad1) -> Net-(U6-SW)
- L2 pad 2: /Antennas/ANT_GNSS_C1 -> NVMe_3V3
- L4 pad 1: /Cameras/CAM1_3V3_0 -> /Cameras/CAM0_3V3_0
- L4 pad 2: CAM1_3V3 -> CAM0_3V3
- L5 pad 1: Net-(U4-SW) -> /Cameras/CAM0_3V3_1
- L5 pad 2: CAM1_3V3 -> CAM0_3V3
- L6 pad 1: /Cameras/CAM0_3V3_0 -> /Cameras/CAM1_3V3_0
- L6 pad 2: CAM0_3V3 -> CAM1_3V3
- L7 pad 1: /Cameras/CAM0_3V3_1 -> /Cameras/CAM1_3V3_1
- L7 pad 2: CAM0_3V3 -> CAM1_3V3
- L8 pad 1: /Cameras/CAM1_3V3_1 -> Net-(C73-Pad1)
- L8 pad 2: CAM1_3V3 -> /Antennas/ANT_GNSS_C1
- LED1 pad 1: Net-(LED1-K) -> GND
- LED1 pad 2: VREG_3V8 -> Net-(LED1-A)
- LED3 pad 1: GND -> Flash LED
- LED3 pad 2: Net-(LED3-A) -> Flash LED
- LED4 pad 1: Flash LED -> GND
- LED4 pad 2: Flash LED -> Net-(LED4-A)
- Q10 pad 2: GND -> /MCU/MCU_UART_TX
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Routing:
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- added copper zone on B.Cu, net 3V8
- added copper zone on In4.Cu, net 3V8
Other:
- board size 80 x 97.3 mm -> 126.2 x 49.2 mm
- board text removed: "3V3"
- board text removed: "5-12VDC"
- board text removed: "ADC"
- board text removed: "BAT"
- board text removed: "DBG_RX"
- board text removed: "DBG_TX"
- board text removed: "Div"
- board text removed: "GND"
- board text removed: "GNSS"
- board text removed: "IN1"
- board text removed: "IN2"
- board text removed: "IN3"
- board text removed: "LDO17A_3V"
- board text removed: "LTE"
- board text removed: "OUT1"
- board text removed: "OUT2"
- board text removed: "OUT3"
- board text removed: "OUT4"
- board text removed: "RX"
- board text removed: "SCL"
- board text removed: "SDA"
- board text removed: "TX"
- board text removed: "UART1"
- board text removed: "USB_BOOT"
- board text removed: "VREG_3V3"
- board text removed: "WiFi/BT"

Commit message: feat(layout): Completed Placement v2
Includes:
- 3V8 DC-DC converter moved to the top layer
- SIM and SD card positions rearranged
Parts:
- removed J24: ~, 000MCLib:CONN-SMD_1.25-4PLT
- added TP46: TestPoint, TestPoint:TestPoint_Pad_D1.0mm, B.Cu at (145.4, 98.6)
- added TP47: TestPoint, TestPoint:TestPoint_Pad_D1.0mm, B.Cu at (143.4, 98.6)
- added TP48: TestPoint, TestPoint:TestPoint_Pad_D1.0mm, B.Cu at (141.4, 98.6)
- added TP49: TestPoint, TestPoint:TestPoint_Pad_D1.0mm, B.Cu at (141.4, 100.9)
- C1, C17, C18, C19, C2, C20, C23, C24, C3, C4, C6, C9, D2, D3, D4, L1, LED1, R11, R3, R4, R5, TP9, U2: moved to F.Cu
- C36, C66, C68, D13, D23, TP12, TP3, TP31, TP4: moved to B.Cu
- moved C58 223.3 mm to (74.0, 79.1), turned to 180 degrees
- moved C25 42.1 mm to (84.1, 66.5)
- moved C33 42.1 mm to (81.3, 70.1)
- moved IC2 42.1 mm to (80.8, 66.6)
- moved TP10 42.1 mm to (84.6, 70.0)
- moved R12 42.1 mm to (79.9, 62.4)
- moved R14 42.1 mm to (82.9, 63.1)
- moved R15 42.1 mm to (78.2, 65.6)
- moved TP9 38.8 mm to (104.4, 92.2)
- moved TP11 38.5 mm to (88.2, 62.8)
- moved C34 34.7 mm to (91.5, 62.8), turned to 0 degrees
- moved C26 32.6 mm to (88.6, 66.3), turned to 90 degrees
- moved C4 31.1 mm to (92.4, 106.9), turned to 0 degrees
- moved C3 30.6 mm to (92.9, 105.1), turned to 0 degrees
- moved IC3 28.1 mm to (92.0, 66.4), turned to -90 degrees
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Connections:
- net Net-(U12-USB_DM) renamed /MCU/MCU_USB_N
- net Net-(U12-USB_DP) renamed /MCU/MCU_USB_P
- U12 pad 15: /MCU/GPIO12 -> Net-(U12-GPIO12)
- U12 pad 16: /MCU/GPIO13 -> Net-(U12-GPIO13)
- U12 pad 17: /MCU/GPIO14 -> Net-(U12-GPIO14)
- U12 pad 18: /MCU/GPIO15 -> Net-(U12-GPIO15)
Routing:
- net /SIM_SD/USIM1_DET: track 0.00 -> 70.9 mm, vias 0 -> 2
- net /MCU/MCU_USB_P: track 0.00 -> 66.5 mm, vias 0 -> 2
- net /MCU/MCU_USB_N: track 0.00 -> 65.8 mm, vias 0 -> 2
- net Net-(U1F-USIM1_RST): track 0.00 -> 60.3 mm, vias 0 -> 2
- net /SIM_SD/USIM1_VDD: track 0.00 -> 59.6 mm, vias 0 -> 2
- net Net-(U1F-USIM1_DATA): track 0.00 -> 51.8 mm
- net Net-(U1F-USIM1_CLK): track 0.00 -> 50.4 mm
- net Net-(J14-DAT0): track 0.00 -> 40.0 mm, vias 0 -> 2
- net Net-(J14-DAT1): track 0.00 -> 38.4 mm, vias 0 -> 2
- net Net-(J14-CLK): track 0.00 -> 34.7 mm, vias 0 -> 2
- net Net-(J14-CMD): track 0.00 -> 32.5 mm, vias 0 -> 2
- net Net-(J14-DAT2): track 0.00 -> 29.9 mm, vias 0 -> 2
- net Net-(J14-CD/DAT3): track 0.00 -> 29.6 mm, vias 0 -> 2
- net Net-(U1F-SD_CLK): track 0.00 -> 23.5 mm
- net Net-(U1F-SD_CMD): track 0.00 -> 21.0 mm
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- added copper zone on F.Cu, net 3V8
- added copper zone on F.Cu, net Net-(C36-+)
- added copper zone on B.Cu, net Net-(D2-K)
- added copper zone on F.Cu, net Net-(D2-K)
- added copper zone on In4.Cu, net Net-(D2-K)
- added copper zone on F.Cu, net Net-(U2-SW)
- added copper zone on B.Cu, net TypeC_VBUS
- added copper zone on F.Cu, net TypeC_VBUS
- added copper zone on In4.Cu, net TypeC_VBUS
- added copper zone on F.Cu, net VBAT
- added copper zone on In4.Cu, net VBAT

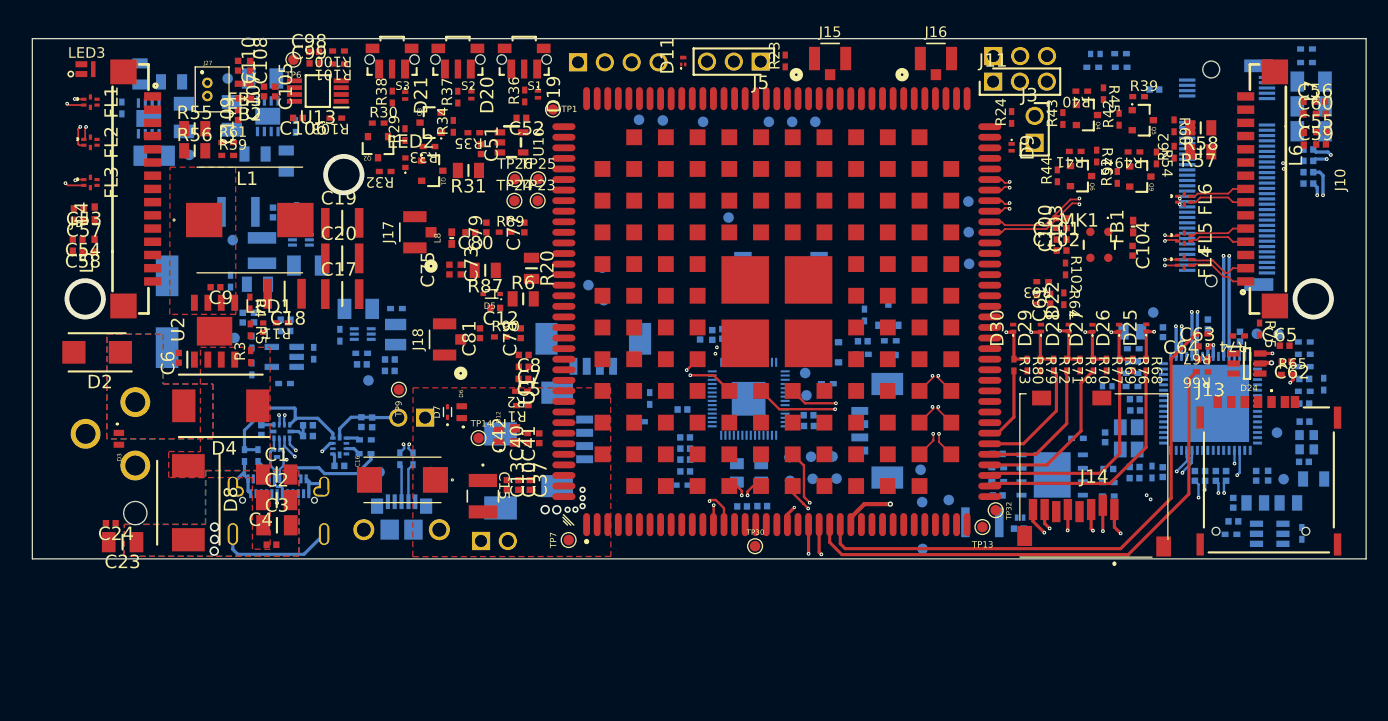
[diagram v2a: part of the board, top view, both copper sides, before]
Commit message: feat(layout): Routed DP traces
Includes:
- Routed DP Camera/USB/PCIe
- Routed SIM/SD
- Routed ASM
- Routed RP
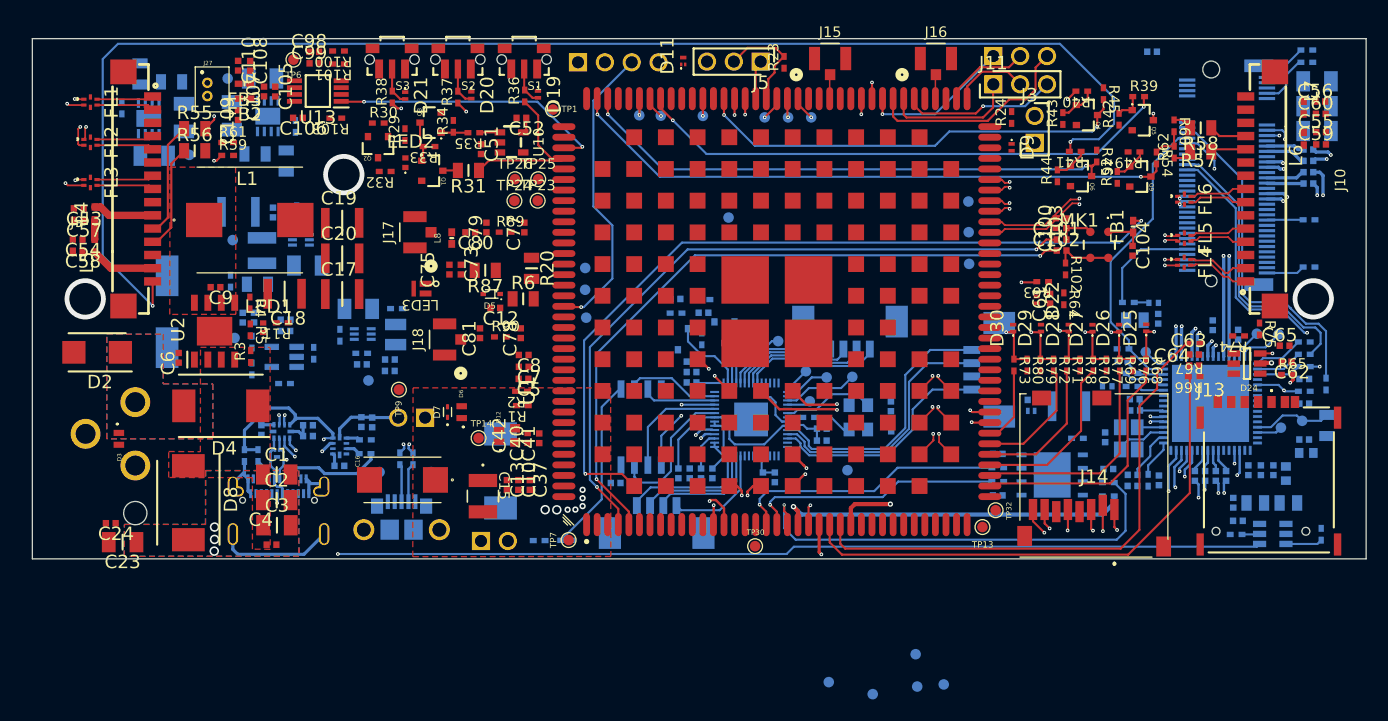
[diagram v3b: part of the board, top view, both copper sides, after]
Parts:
- moved J4 39.8 mm to (159.9, 90.4), turned to 90 degrees
- moved LED3 38.7 mm to (106.9, 82.7), turned to 180 degrees
- moved R123 25.9 mm to (190.5, 80.6), turned to 180 degrees
- moved R120 25.0 mm to (190.5, 76.2), turned to 180 degrees
- moved LED4 24.2 mm to (175.8, 84.0), turned to -90 degrees
- moved R119 23.6 mm to (173.4, 84.0), turned to 180 degrees
- moved C96 21.0 mm to (130.6, 83.7), turned to 0 degrees
- moved R96 20.4 mm to (130.6, 85.0), turned to 180 degrees
- moved Q10 20.0 mm to (130.8, 87.5), turned to 0 degrees
- moved IC1 19.5 mm to (127.3, 95.8), turned to -90 degrees
- moved TP45 19.3 mm to (145.1, 119.9)
- moved TP17 17.5 mm to (153.3, 117.3)
- moved TP5 17.5 mm to (153.5, 120.3)
- moved TP12 17.5 mm to (156.0, 120.1)
- moved R91 17.0 mm to (117.7, 106.5), turned to 180 degrees
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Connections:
- net /NVMe/REFCLKn renamed /NVMe/REFCLK_N
- net /NVMe/REFCLKp renamed /NVMe/REFCLK_P
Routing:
- net CAM0_IR_CUT_GPIO: track 0.00 -> 134.3 mm, vias 0 -> 2
- net /USB_UARTs/USB_SW: track 15.2 -> 123.5 mm, vias 0 -> 2
- net /Audio/MIC_BIAS1: track 0.00 -> 75.9 mm, vias 0 -> 2
- net /Cameras/CAM0_I2C_SDA: track 0.00 -> 69.1 mm, vias 0 -> 2
- net /Cameras/CAM0_I2C_SCL: track 0.00 -> 66.7 mm, vias 0 -> 2
- net /Audio/MIC1_P: track 0.00 -> 66.3 mm, vias 0 -> 2
- net /Audio/MIC1_M: track 0.00 -> 65.1 mm, vias 0 -> 2
- net /Interfaces/CAM1_IN: track 0.00 -> 57.7 mm, vias 0 -> 2
- net /Interfaces/OUT1: track 0.00 -> 55.9 mm, vias 0 -> 1
- net /Interfaces/GPIO_103: track 0.00 -> 51.2 mm, vias 0 -> 2
- net /Interfaces/CAM0_IN: track 0.00 -> 51.2 mm, vias 0 -> 2
- net /Interfaces/IN1: track 0.00 -> 49.8 mm, vias 0 -> 1
- net /Interfaces/GPIO_31: track 0.00 -> 41.6 mm, vias 0 -> 2
- net /NVMe/REFCLK_P: track 0.00 -> 40.6 mm, vias 0 -> 2
- net /SIM_SD/USIM2_DATA: track 1.89 -> 42.3 mm
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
